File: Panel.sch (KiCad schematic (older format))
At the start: 11 parts, among them J7 Rotated_Barrel, U7 LM3406HV

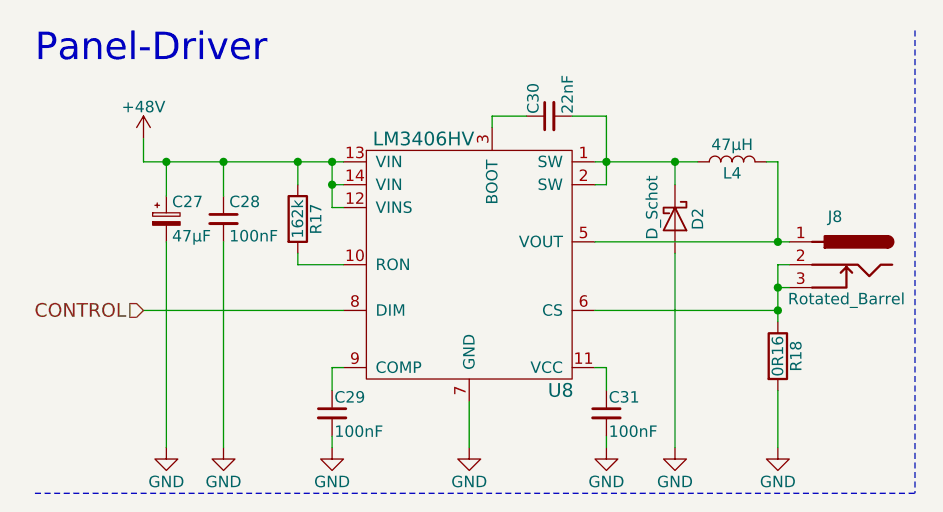
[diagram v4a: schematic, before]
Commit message: Added the Elec-Footprint to the Panel
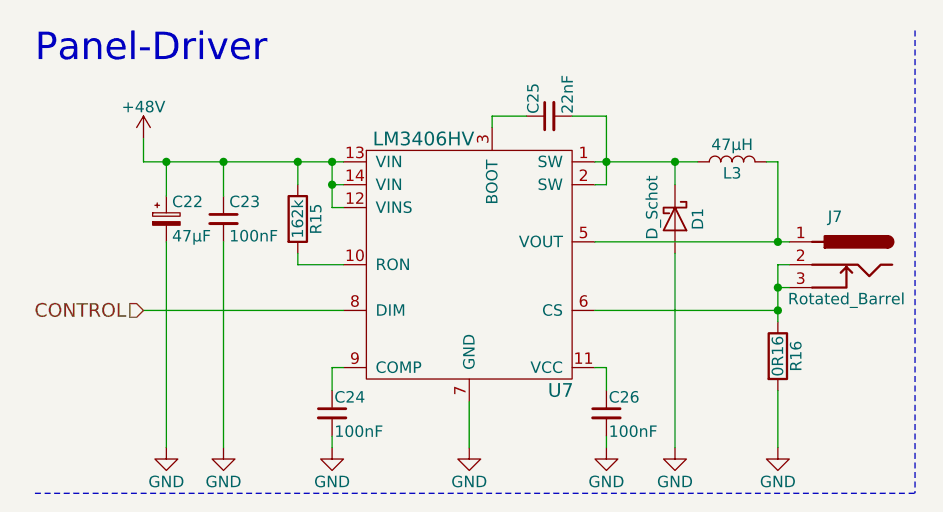
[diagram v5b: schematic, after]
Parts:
- C22: footprint (none) -> CP_Elec:CP_Elec_8.3x8.3mm_P6.5mm_D8mm
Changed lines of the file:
@@
 $Descr A4 11693 8268
 encoding utf-8
-Sheet 4 7
+Sheet 3 7
 Title ""
 Date "2018-02-14"
@@
 AR Path="/5A4C34AF/5A7753B7" Ref="R15"  Part="1"
 AR Path="/5A4C3F5F/5A7753B7" Ref="R17"  Part="1"
-F 0 "R17" V 1705 1300 50  0000 C CNN
+F 0 "R15" V 1705 1300 50  0000 C CNN
 F 1 "162k" V 1625 1300 50  0000 C CNN
 F 2 "Resistor_SMD:R_0603_1608Metric" V 1555 1300 50  0001 C CNN
@@
 AR Path="/5A4C34AF/5A77745B" Ref="C24"  Part="1"
 AR Path="/5A4C3F5F/5A77745B" Ref="C29"  Part="1"
-F 0 "C29" H 1785 2220 50  0000 L CNN
+F 0 "C24" H 1785 2220 50  0000 L CNN
 F 1 "100nF" H 1785 2070 50  0000 L CNN
 F 2 "Capacitor_SMD:C_0805_2012Metric" H 1775 2150 50  0001 C CNN
@@
 AR Path="/5A4C34AF/5A777BDD" Ref="#PWR063"  Part="1"
 AR Path="/5A4C3F5F/5A777BDD" Ref="#PWR071"  Part="1"
-F 0 "#PWR071" H 1775 2050 50  0001 C CNN
+F 0 "#PWR063" H 1775 2050 50  0001 C CNN
 F 1 "GND" H 1775 2150 50  0000 C CNN
 F 2 "" H 1775 2300 50  0001 C CNN
@@
 AR Path="/5A4C34AF/5A777CD4" Ref="C26"  Part="1"
 AR Path="/5A4C3F5F/5A777CD4" Ref="C31"  Part="1"
-F 0 "C31" H 2985 2220 50  0000 L CNN
+F 0 "C26" H 2985 2220 50  0000 L CNN
 F 1 "100nF" H 2985 2070 50  0000 L CNN
 F 2 "Capacitor_SMD:C_0805_2012Metric" H 2975 2150 50  0001 C CNN
@@
 AR Path="/5A4C34AF/5A777CDA" Ref="#PWR065"  Part="1"
 AR Path="/5A4C3F5F/5A777CDA" Ref="#PWR073"  Part="1"
-F 0 "#PWR073" H 2975 2050 50  0001 C CNN
+F 0 "#PWR065" H 2975 2050 50  0001 C CNN
 F 1 "GND" H 2975 2150 50  0000 C CNN
 F 2 "" H 2975 2300 50  0001 C CNN
@@
 AR Path="/5A4C34AF/5A777FA3" Ref="#PWR064"  Part="1"
 AR Path="/5A4C3F5F/5A777FA3" Ref="#PWR072"  Part="1"
-F 0 "#PWR072" H 2375 2050 50  0001 C CNN
+F 0 "#PWR064" H 2375 2050 50  0001 C CNN
 F 1 "GND" H 2375 2150 50  0000 C CNN
 F 2 "" H 2375 2300 50  0001 C CNN
@@
 AR Path="/5A4C34AF/5A77816D" Ref="C25"  Part="1"
 AR Path="/5A4C3F5F/5A77816D" Ref="C30"  Part="1"
-F 0 "C30" H 2735 920 50  0000 L CNN
+F 0 "C25" H 2735 920 50  0000 L CNN
 F 1 "22nF" H 2735 770 50  0000 L CNN
 F 2 "Capacitor_SMD:C_0603_1608Metric" H 2725 850 50  0001 C CNN
@@
 AR Path="/5A4C34AF/5A77899A" Ref="L3"  Part="1"
 AR Path="/5A4C3F5F/5A77899A" Ref="L4"  Part="1"
-F 0 "L4" V 3475 1050 50  0000 C CNN
+F 0 "L3" V 3475 1050 50  0000 C CNN
 F 1 "47μH" V 3600 1050 50  0000 C CNN
 F 2 "" H 3525 1050 50  0001 C CNN
@@
 AR Path="/5A4C34AF/5A7789F9" Ref="D1"  Part="1"
 AR Path="/5A4C3F5F/5A7789F9" Ref="D2"  Part="1"
-F 0 "D2" H 3275 1400 50  0000 C CNN
+F 0 "D1" H 3275 1400 50  0000 C CNN
 F 1 "D_Schot" H 3225 1200 50  0000 C CNN
 F 2 "Diode_SMD:D_SMA_Handsoldering" H 3275 1300 50  0001 C CNN
@@
 AR Path="/5A4C34AF/5A778B62" Ref="#PWR066"  Part="1"
 AR Path="/5A4C3F5F/5A778B62" Ref="#PWR074"  Part="1"
-F 0 "#PWR074" H 3275 2050 50  0001 C CNN
+F 0 "#PWR066" H 3275 2050 50  0001 C CNN
 F 1 "GND" H 3275 2150 50  0000 C CNN
 F 2 "" H 3275 2300 50  0001 C CNN
@@
 AR Path="/5A4C34AF/5A779AD3" Ref="J7"  Part="1"
 AR Path="/5A4C3F5F/5A779AD3" Ref="J8"  Part="1"
-F 0 "J8" H 3975 1710 50  0000 C CNN
+F 0 "J7" H 3975 1710 50  0000 C CNN
 F 1 "Rotated_Barrel" H 4025 1350 50  0000 C CNN
 F 2 "" H 4025 1440 50  0001 C CNN
@@
 AR Path="/5A4C34AF/5A77A2E1" Ref="R16"  Part="1"
 AR Path="/5A4C3F5F/5A77A2E1" Ref="R18"  Part="1"
-F 0 "R18" V 3805 1900 50  0000 C CNN
+F 0 "R16" V 3805 1900 50  0000 C CNN
 F 1 "0R16" V 3725 1900 50  0000 C CNN
 F 2 "Resistor_SMD:R_1206_3216Metric" V 3655 1900 50  0001 C CNN
@@
 AR Path="/5A4C34AF/5A77A9CB" Ref="#PWR067"  Part="1"
 AR Path="/5A4C3F5F/5A77A9CB" Ref="#PWR075"  Part="1"
-F 0 "#PWR075" H 3725 2050 50  0001 C CNN
+F 0 "#PWR067" H 3725 2050 50  0001 C CNN
 F 1 "GND" H 3725 2150 50  0000 C CNN
 F 2 "" H 3725 2300 50  0001 C CNN
@@
 AR Path="/5A4C34AF/5A77D43C" Ref="#PWR062"  Part="1"
 AR Path="/5A4C3F5F/5A77D43C" Ref="#PWR070"  Part="1"
-F 0 "#PWR070" H 1300 2050 50  0001 C CNN
+F 0 "#PWR062" H 1300 2050 50  0001 C CNN
 F 1 "GND" H 1300 2150 50  0000 C CNN
 F 2 "" H 1300 2300 50  0001 C CNN
@@
 AR Path="/5A4C34AF/5A77E620" Ref="U7"  Part="1"
 AR Path="/5A4C3F5F/5A77E620" Ref="U8"  Part="1"
-F 0 "U8" H 2775 950 60  0000 C CNN
+F 0 "U7" H 2775 950 60  0000 C CNN
 F 1 "LM3406HV" H 2175 2050 60  0000 C CNN
 F 2 "" H 2375 2100 60  0001 C CNN
@@
 AR Path="/5A4C34AF/5A84C99A" Ref="#PWR060"  Part="1"
 AR Path="/5A4C3F5F/5A84C99A" Ref="#PWR068"  Part="1"
-F 0 "#PWR068" H 950 800 50  0001 C CNN
+F 0 "#PWR060" H 950 800 50  0001 C CNN
 F 1 "+48V" H 950 1090 50  0000 C CNN
 F 2 "" H 950 950 50  0001 C CNN
@@
 AR Path="/5A4C34AF/5ABA3DDA" Ref="C22"  Part="1"
 AR Path="/5A4C3F5F/5ABA3DDA" Ref="C27"  Part="1"
-F 0 "C27" H 1075 1375 50  0000 L CNN
+F 0 "C22" H 1075 1375 50  0000 L CNN
 F 1 "47μF" H 1075 1225 50  0000 L CNN
-F 2 "" H 1050 1300 50  0001 C CNN
+F 2 "CP_Elec:CP_Elec_8.3x8.3mm_P6.5mm_D8mm" H 1050 1300 50  0001 C CNN
 F 3 "~" H 1050 1300 50  0001 C CNN
 F 4 "https://www.digikey.com/product-detail/en/panasonic-electronic-components/EEE-TG1J470UP/PCE4093CT-ND/817764" H 1050 1300 50  0001 C CNN "Buy"
@@
 AR Path="/5A4C34AF/5ABA5E6C" Ref="C23"  Part="1"
 AR Path="/5A4C3F5F/5ABA5E6C" Ref="C28"  Part="1"
-F 0 "C28" H 1325 1375 50  0000 L CNN
+F 0 "C23" H 1325 1375 50  0000 L CNN
 F 1 "100nF" H 1325 1225 50  0000 L CNN
 F 2 "Capacitor_SMD:C_0805_2012Metric" H 1300 1300 50  0001 C CNN
@@
 AR Path="/5A4C34AF/5ABA815F" Ref="#PWR061"  Part="1"
 AR Path="/5A4C3F5F/5ABA815F" Ref="#PWR069"  Part="1"
-F 0 "#PWR069" H 1050 2050 50  0001 C CNN
+F 0 "#PWR061" H 1050 2050 50  0001 C CNN
 F 1 "GND" H 1050 2150 50  0000 C CNN
 F 2 "" H 1050 2300 50  0001 C CNN

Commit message: Associated the LED-Buckinductor
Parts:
- L3: footprint (none) -> I_SMD:I_SMD_Bourne_12.7x12.7mm
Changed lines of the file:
@@
 AR Path="/5A4C34AF/5A777BDD" Ref="#PWR063"  Part="1"
 AR Path="/5A4C3F5F/5A777BDD" Ref="#PWR071"  Part="1"
-F 0 "#PWR071" H 1775 2050 50  0001 C CNN
+F 0 "#PWR063" H 1775 2050 50  0001 C CNN
 F 1 "GND" H 1775 2150 50  0000 C CNN
 F 2 "" H 1775 2300 50  0001 C CNN
@@
 AR Path="/5A4C34AF/5A777CDA" Ref="#PWR065"  Part="1"
 AR Path="/5A4C3F5F/5A777CDA" Ref="#PWR073"  Part="1"
-F 0 "#PWR073" H 2975 2050 50  0001 C CNN
+F 0 "#PWR065" H 2975 2050 50  0001 C CNN
 F 1 "GND" H 2975 2150 50  0000 C CNN
 F 2 "" H 2975 2300 50  0001 C CNN
@@
 AR Path="/5A4C34AF/5A777FA3" Ref="#PWR064"  Part="1"
 AR Path="/5A4C3F5F/5A777FA3" Ref="#PWR072"  Part="1"
-F 0 "#PWR072" H 2375 2050 50  0001 C CNN
+F 0 "#PWR064" H 2375 2050 50  0001 C CNN
 F 1 "GND" H 2375 2150 50  0000 C CNN
 F 2 "" H 2375 2300 50  0001 C CNN
@@
 F 0 "L3" V 3475 1050 50  0000 C CNN
 F 1 "47μH" V 3600 1050 50  0000 C CNN
-F 2 "" H 3525 1050 50  0001 C CNN
+F 2 "I_SMD:I_SMD_Bourne_12.7x12.7mm" H 3525 1050 50  0001 C CNN
 F 3 "" H 3525 1050 50  0001 C CNN
 F 4 "https://www.digikey.com/product-detail/en/bourns-inc/SRR1208-470YL/SRR1208-470YLCT-ND/2353025" V 3525 1050 60  0001 C CNN "Buy"
@@
 AR Path="/5A4C34AF/5A778B62" Ref="#PWR066"  Part="1"
 AR Path="/5A4C3F5F/5A778B62" Ref="#PWR074"  Part="1"
-F 0 "#PWR074" H 3275 2050 50  0001 C CNN
+F 0 "#PWR066" H 3275 2050 50  0001 C CNN
 F 1 "GND" H 3275 2150 50  0000 C CNN
 F 2 "" H 3275 2300 50  0001 C CNN
@@
 AR Path="/5A4C34AF/5A77A9CB" Ref="#PWR067"  Part="1"
 AR Path="/5A4C3F5F/5A77A9CB" Ref="#PWR075"  Part="1"
-F 0 "#PWR075" H 3725 2050 50  0001 C CNN
+F 0 "#PWR067" H 3725 2050 50  0001 C CNN
 F 1 "GND" H 3725 2150 50  0000 C CNN
 F 2 "" H 3725 2300 50  0001 C CNN
@@
 AR Path="/5A4C34AF/5A77D43C" Ref="#PWR062"  Part="1"
 AR Path="/5A4C3F5F/5A77D43C" Ref="#PWR070"  Part="1"
-F 0 "#PWR070" H 1300 2050 50  0001 C CNN
+F 0 "#PWR062" H 1300 2050 50  0001 C CNN
 F 1 "GND" H 1300 2150 50  0000 C CNN
 F 2 "" H 1300 2300 50  0001 C CNN
@@
 AR Path="/5A4C34AF/5A84C99A" Ref="#PWR060"  Part="1"
 AR Path="/5A4C3F5F/5A84C99A" Ref="#PWR068"  Part="1"
-F 0 "#PWR068" H 950 800 50  0001 C CNN
+F 0 "#PWR060" H 950 800 50  0001 C CNN
 F 1 "+48V" H 950 1090 50  0000 C CNN
 F 2 "" H 950 950 50  0001 C CNN
@@
 AR Path="/5A4C34AF/5ABA815F" Ref="#PWR061"  Part="1"
 AR Path="/5A4C3F5F/5ABA815F" Ref="#PWR069"  Part="1"
-F 0 "#PWR069" H 1050 2050 50  0001 C CNN
+F 0 "#PWR061" H 1050 2050 50  0001 C CNN
 F 1 "GND" H 1050 2150 50  0000 C CNN
 F 2 "" H 1050 2300 50  0001 C CNN

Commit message: Created the Footprint for the LM3406HV and associated it
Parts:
- U7: footprint (none) -> HTSSOP:HTSSOP-14_4.4x5mm_EP3x3.1mm_P0.65mm_ThermalPad
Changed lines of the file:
@@
 F 0 "U7" H 2775 950 60  0000 C CNN
 F 1 "LM3406HV" H 2175 2050 60  0000 C CNN
-F 2 "" H 2375 2100 60  0001 C CNN
+F 2 "HTSSOP:HTSSOP-14_4.4x5mm_EP3x3.1mm_P0.65mm_ThermalPad" H 2375 2100 60  0001 C CNN
 F 3 "http://www.ti.com/lit/ds/symlink/lm3406.pdf" H 2375 2100 60  0001 C CNN
 F 4 "https://www.digikey.com/product-detail/en/texas-instruments/LM3406HVQMHXQ1/296-38110-1-ND/4967315" H 2375 1500 60  0001 C CNN "Buy"
